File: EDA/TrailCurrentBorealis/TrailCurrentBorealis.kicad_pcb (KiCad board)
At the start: 2 copper layers, 77 x 50.5 mm, 13 parts, among them IC1 SN65HVD230DR, J1 DHT22, J2 S4B-XH-SM4-TB, U1 ESP32-S3-Zero, U2 GY-SGP30, U3 Mini560

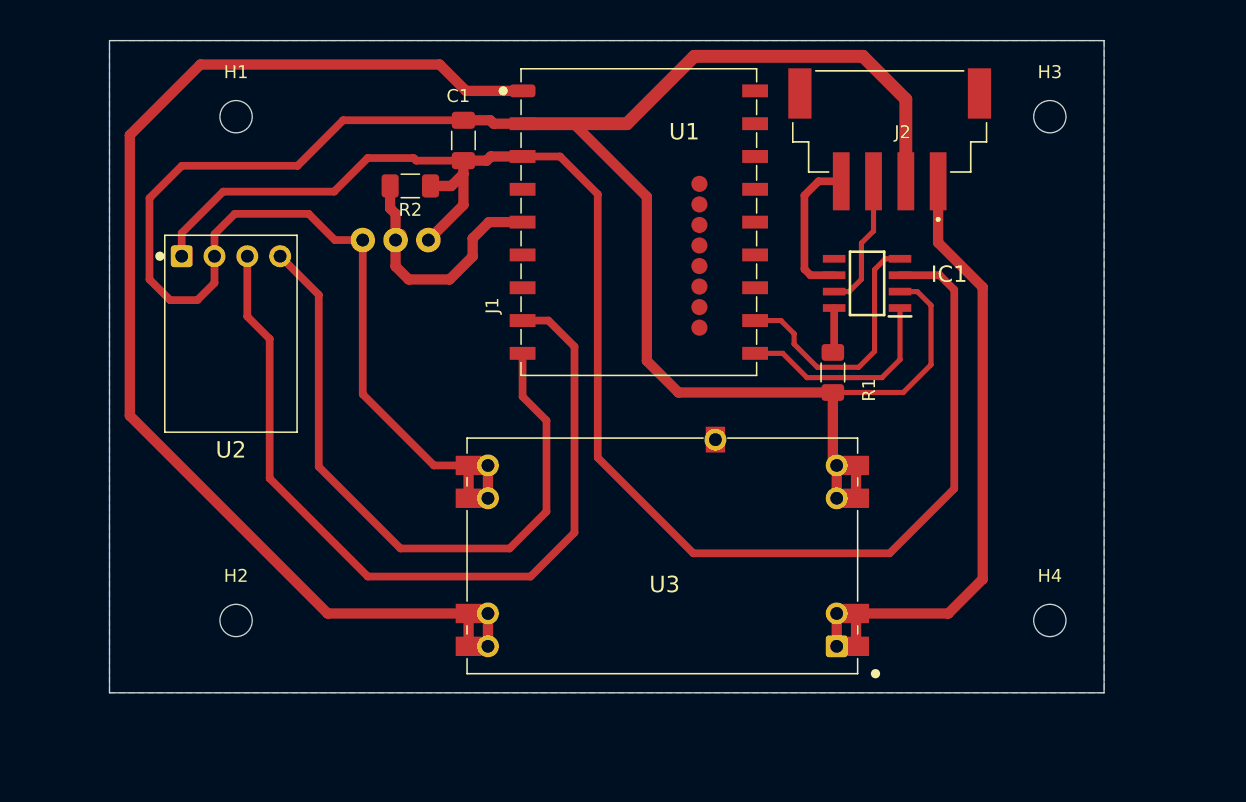
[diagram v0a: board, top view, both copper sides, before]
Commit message: Switching to new temp and humdity sensor
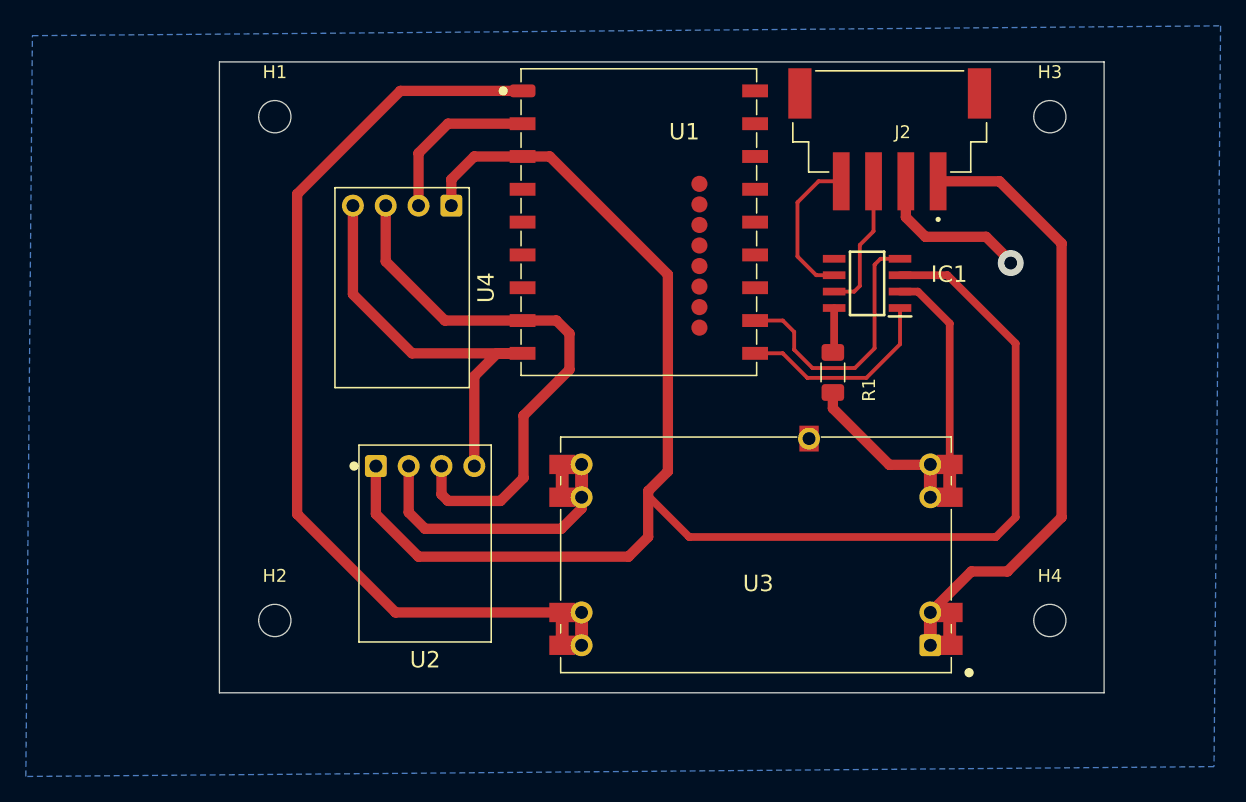
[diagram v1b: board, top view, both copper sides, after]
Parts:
- removed C1: 100nF, Capacitor_SMD:C_1206_3216Metric_Pad1.33x1.80mm_HandSolder
- removed J1: DHT22, Sensor:DHT22_Module
- removed R2: 4.7K, Capacitor_SMD:C_1206_3216Metric_Pad1.33x1.80mm_HandSolder
- added U4: SHT31-D-TempHumidity, TrailCurrentFootprints:SHT31-D-TempHumidity, F.Cu at (101.9, 94.2)
- moved U2 22.1 mm to (103.6, 114.0)
- moved U3 7.25 mm to (129.2, 114.9)
- moved H1 3.00 mm to (92.0, 81.0)
- moved H2 3.00 mm to (92.0, 120.0)
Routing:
- net GND: track 196.2 -> 81.1 mm, vias 0 -> 1
- net SCL: track 65.3 -> 43.0 mm
- net DHT_READING: track 20.0 -> 0.00 mm
- net SDA: track 52.0 -> 33.3 mm
- net +5V: track 92.9 -> 74.3 mm
- net +3.3V: track 122.3 -> 126.4 mm
- net +12V: track 48.2 -> 51.0 mm
- net CAN_TX: track 16.6 -> 15.9 mm
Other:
- board size 77 x 50.5 mm -> 68.5 x 48.8 mm

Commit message: Updated PCB for DIY build
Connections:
- U1 pad 8: SCL -> SDA
- U1 pad 9: SDA -> SCL
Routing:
- net SDA: track 33.3 -> 74.6 mm
- net SCL: track 43.0 -> 61.7 mm
- net +3.3V: track 126.4 -> 111.8 mm
- net GND: track 81.1 -> 83.0 mm
- net CAN_RX: track 20.8 -> 20.2 mm
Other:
- board size 68.5 x 48.8 mm -> 68.5 x 49.1 mm
